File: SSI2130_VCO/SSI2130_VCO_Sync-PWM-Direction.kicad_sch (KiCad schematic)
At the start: 28 parts, among them J2 SYNC_IN, SW1 SW_SPST_LED, SW2 SW_SPST_LED, SW3 SW_SPST_LED, U2 MC74HC4066ADR2G

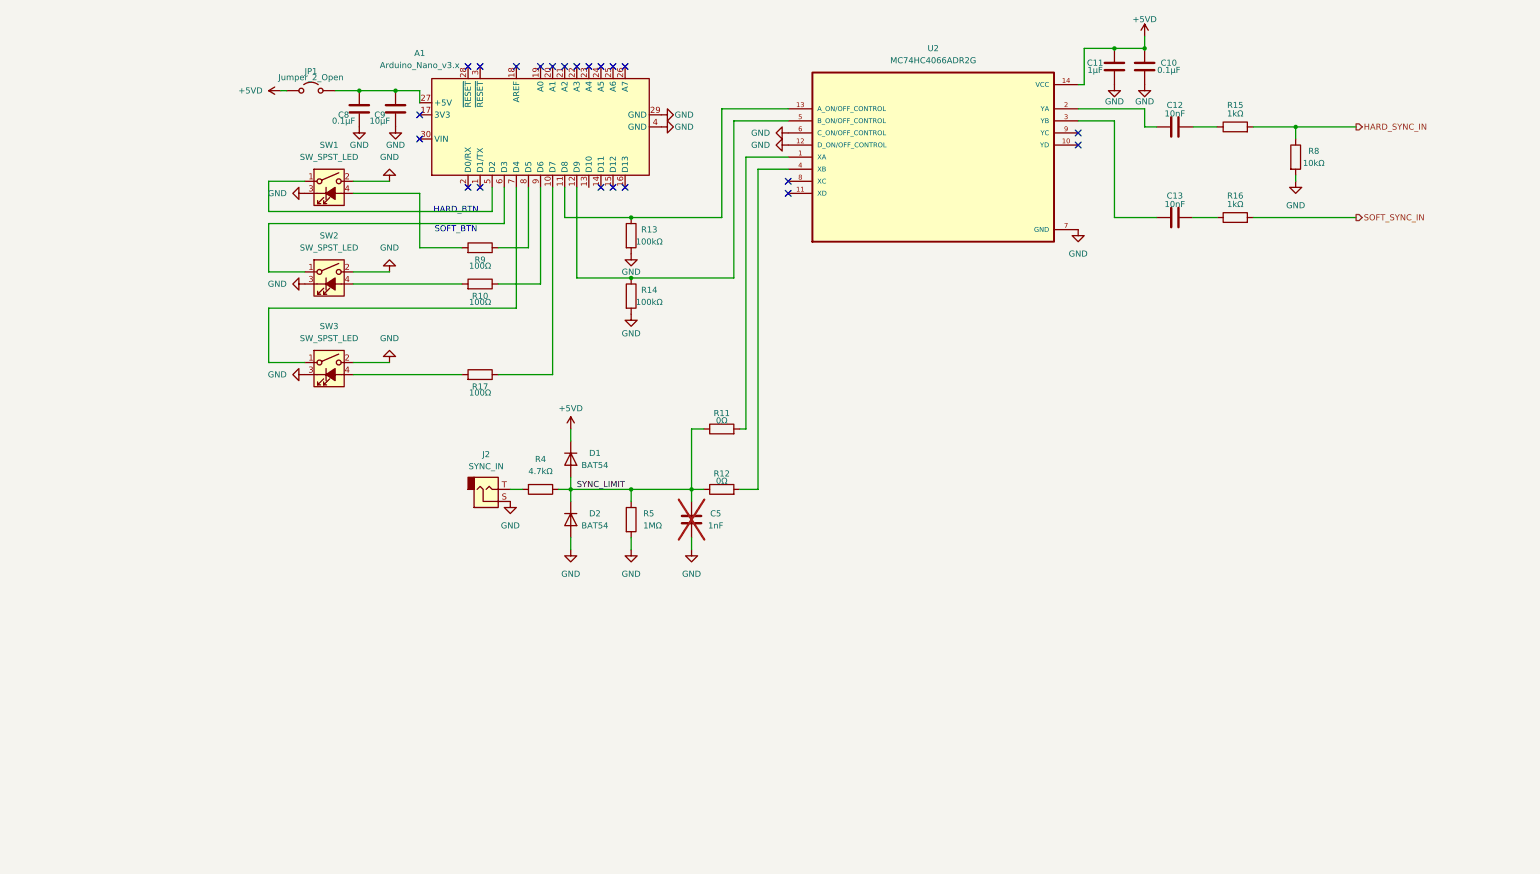
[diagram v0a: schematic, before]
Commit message: fix sync circuit
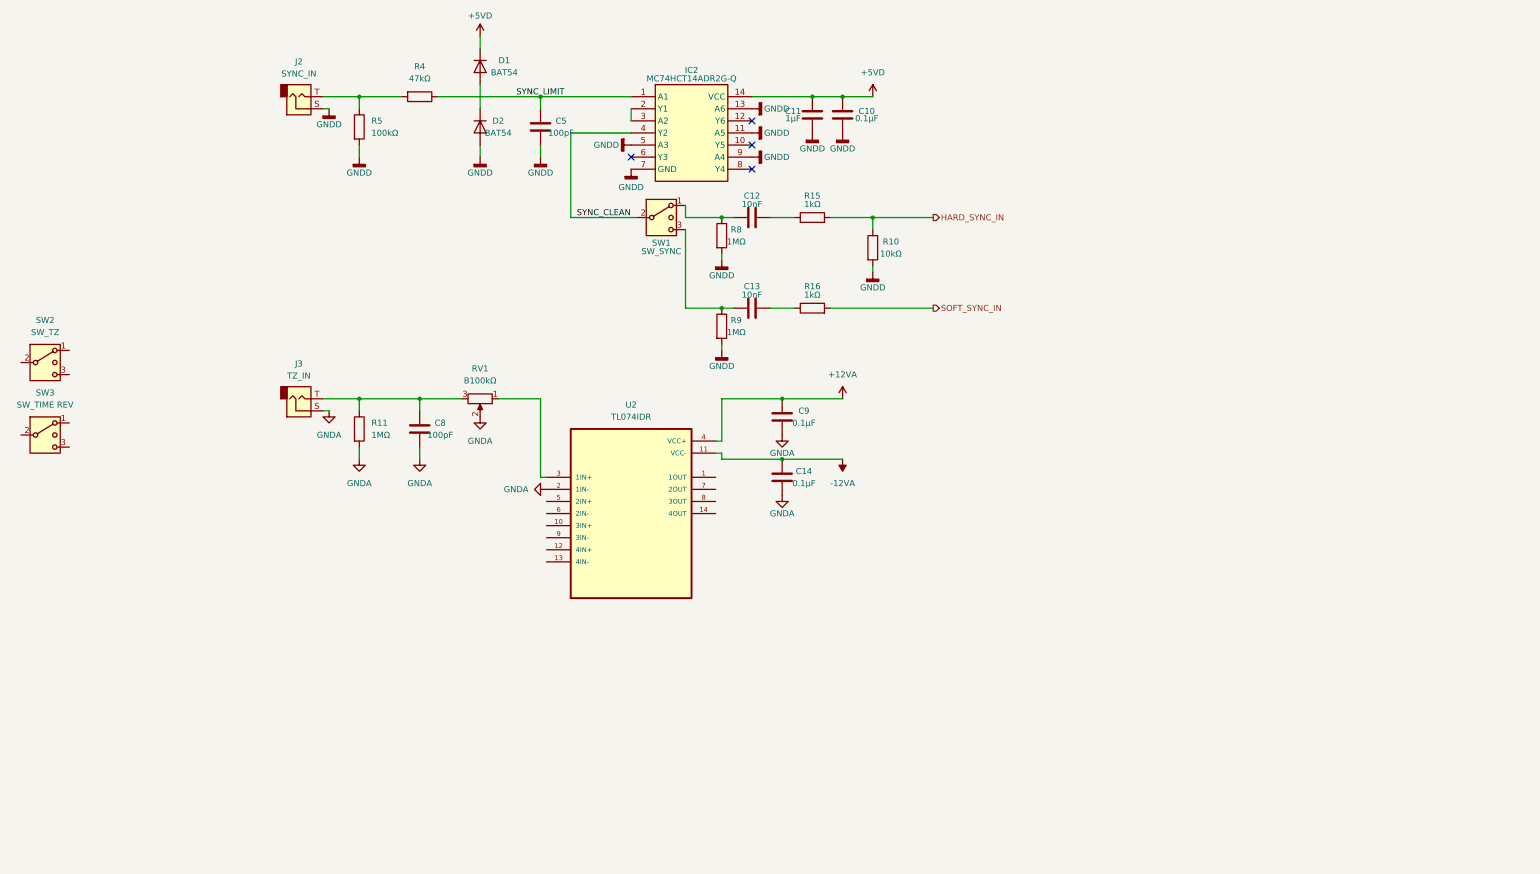
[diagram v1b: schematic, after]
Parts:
- removed A1: Arduino_Nano_v3.x, Module:Arduino_Nano, symbol MCU_Module:Arduino_Nano_v3.x
- removed JP1: Jumper_2_Open, symbol Jumper:Jumper_2_Open
- removed R12: 0Ω, symbol Device:R
- removed R13, R14: 100kΩ, symbol Device:R
- removed R17: 100Ω, symbol Device:R
- removed SW1, SW2, SW3: SW_SPST_LED, symbol Switch:SW_SPST_LED
- removed U2: MC74HC4066ADR2G, MC74HC4066ADR2G:SOIC127P600X175-14N, symbol MC74HC4066ADR2G:MC74HC4066ADR2G
- added C14: 0.1µF, symbol Device:C
- added IC2: MC74HCT14ADR2G-Q, SOIC127P600X175-14N, symbol MC74HCT14ADR2G-Q:MC74HCT14ADR2G-Q
- added J3: TZ_IN, symbol Connector_Audio:AudioJack2
- added RV1: B100kΩ, symbol Device:R_Potentiometer
- added SW1: SW_SYNC, symbol Switch:SW_SPDT_MSM
- added SW2: SW_TZ, symbol Switch:SW_SPDT_MSM
- added SW3: SW_TIME REV, symbol Switch:SW_SPDT_MSM
- added U2: TL074IDR, TL074IDR:SOIC127P600X175-14N, symbol TL074IDR:TL074IDR
- C5: value 1nF -> 100pF; now fitted
- C8: value 0.1µF -> 100pF
- C9: value 10µF -> 0.1µF
- R10: value 100Ω -> 10kΩ
- R11: value 0Ω -> 1MΩ
- R4: value 4.7kΩ -> 47kΩ
- R5: value 1MΩ -> 100kΩ
- R8: value 10kΩ -> 1MΩ
- R9: value 100Ω -> 1MΩ
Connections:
- net +5VD: now also IC2.14 (VCC)
- net HARD_SYNC_IN: now also R10.1; no longer R8.1
- net SYNC_LIMIT: now also IC2.1 (A1); no longer D1.2 (A), D2.1 (K), R11.1, R5.1
- net GNDA: now reaches R11.2
- net GNDA: now also C8.2, C9.2, C14.2, J3.S, RV1.2, U2.2 (1IN-)
- net GNDD: now reaches R9.2
- net GNDD: now also C10.1, C11.1, C5.2, D2.2 (A), J2.S, R10.2, R5.2, R8.2, IC2.11 (A5), IC2.13 (A6), IC2.5 (A3), IC2.7 (GND), IC2.9 (A4)
- net at J2.T, R4.2: now also R5.1
- net at C12.2: now also R8.1, SW1.1
- net at C13.2: now also R9.1, SW1.3 (4)
- net at C8.1: now also R11.1, J3.T, RV1.3; no longer C9.1
- removed net GND: C10.1, C11.1, C5.2, C8.2, C9.2, D2.2 (A), J2.S, R5.2, R8.2
- new net: D1.2 (A), D2.1 (K)
- new net: RV1.1, U2.3 (1IN+)
- new net: IC2.2 (Y1), IC2.3 (A2)
- new net +12VA: C9.1, U2.4 (VCC+)
- new net -12VA: C14.1, U2.11 (VCC-)
- new net SYNC_CLEAN: IC2.4 (Y2), SW1.2 (3)
- no-connect marks 22 -> 4
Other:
- note removed: "HARD_BTN"
- note removed: "SOFT_BTN"
- moved on the sheet: D1, D2, J2, R4

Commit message: add TZ circuit
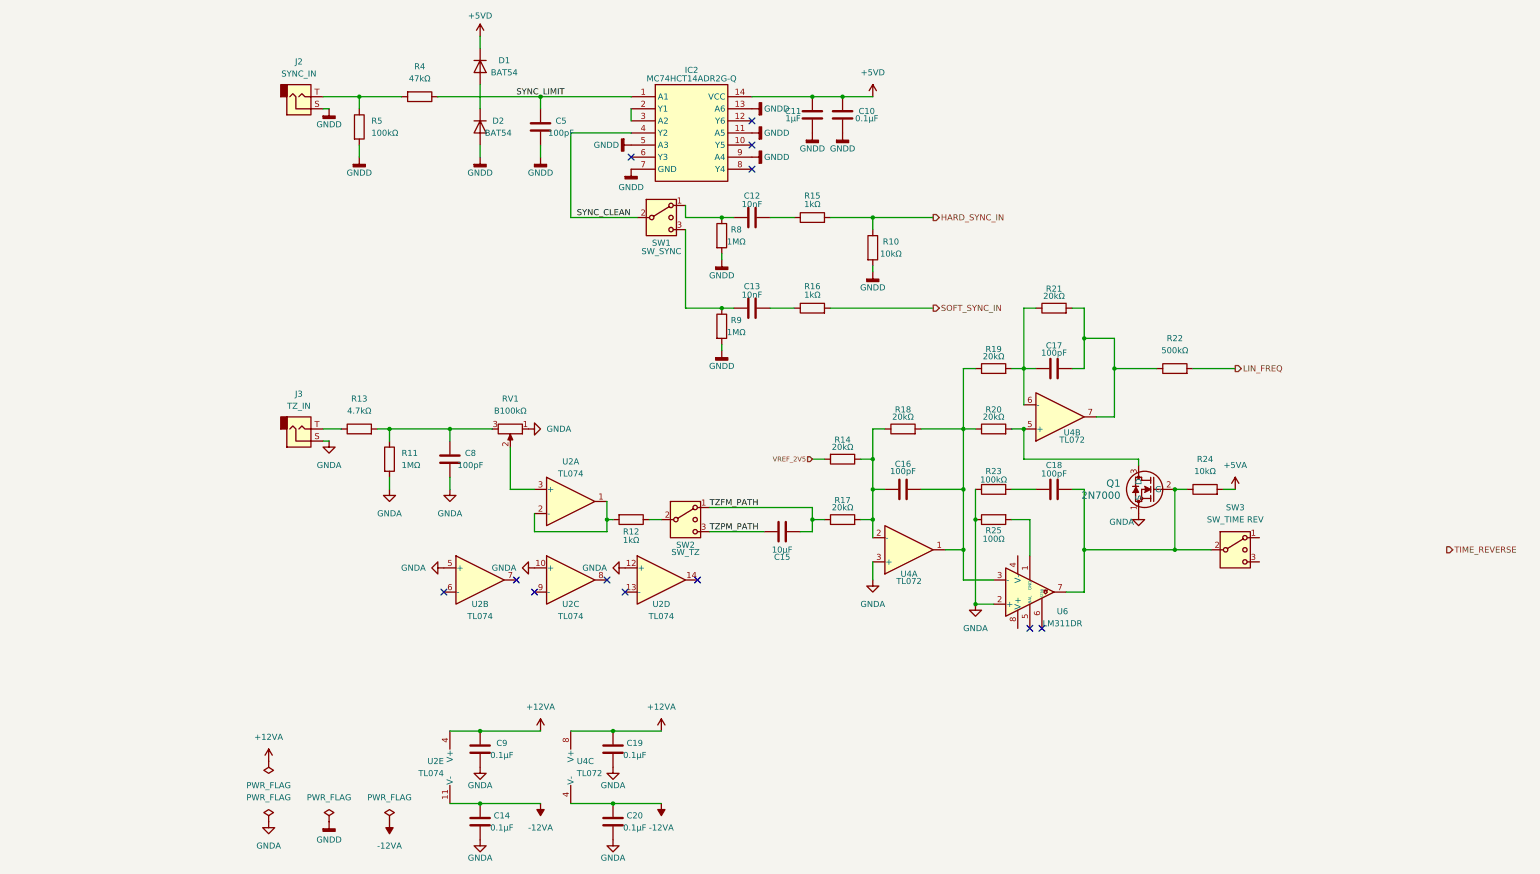
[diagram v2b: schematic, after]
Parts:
- removed U2: TL074IDR, TL074IDR:SOIC127P600X175-14N, symbol TL074IDR:TL074IDR
- added C15: 10µF, symbol Device:C
- added C16, C17, C18: 100pF, symbol Device:C
- added C19, C20: 0.1µF, symbol Device:C
- added Q1: 2N7000, symbol 2N7000:2N7000
- added R12: 1kΩ, symbol Device:R
- added R13: 4.7kΩ, symbol Device:R
- added R14, R17, R18, R19, R20, R21: 20kΩ, symbol Device:R
- added R22: 500kΩ, symbol Device:R
- added R23: 100kΩ, symbol Device:R
- added R24: 10kΩ, symbol Device:R
- added R25: 100Ω, symbol Device:R
- added U2: TL074, symbol Amplifier_Operational:TL074
- added U4: TL072, symbol Amplifier_Operational:TL072
- added U6: LM311DR, symbol Comparator:LM311
- IC2: footprint SOIC127P600X175-14N -> (none)
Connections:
- net +12VA: now also C19.1, U2.4 (V+), U4.8 (V+)
- net -12VA: now also C20.1, U2.11 (V-), U4.4 (V-)
- net GNDA: now also RV1.1, C19.2, C20.2, Q1.1 (S), R23.1, R25.1, U2.10 (+), U2.12 (+), U2.5 (+), U4.3 (+), U6.2 (+); no longer RV1.2
- net TZFM_PATH: now reaches SW2.1
- net TZFM_PATH: now also C15.2, R17.1
- net at SW2.2 (3): now also R12.1
- net TZPM_PATH: now reaches SW2.3 (4)
- net TZPM_PATH: now also C15.1
- net at C8.1, R11.1, RV1.3: now also R13.2; no longer J3.T
- net at SW3.2 (3): now also C18.2, Q1.2 (G), R24.1, U6.7
- new net: R12.2, U2.1, U2.2 (-)
- new net: C17.1, R19.2, R21.1, U4.6 (-)
- new net: C17.2, R21.2, R22.1, U4.7
- new net: R25.2, U6.1 (GND)
- new net: C16.2, R18.2, R19.1, R20.1, U4.1, U6.3 (-)
- new net: RV1.2, U2.3 (+)
- new net: C18.1, R23.2
- new net: C16.1, R14.1, R17.2, R18.1, U4.2 (-)
- new net: Q1.3 (D), R20.2, U4.5 (+)
- new net: J3.T, R13.1
- new net +5VA: R24.2
- new net LIN_FREQ: R22.2
- new net VREF_2V5: R14.2
- no-connect marks 4 -> 12
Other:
- moved on the sheet: C14, C8, C9, J3, R11, RV1, SW2
